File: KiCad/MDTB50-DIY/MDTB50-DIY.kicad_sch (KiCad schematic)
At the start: 18 parts

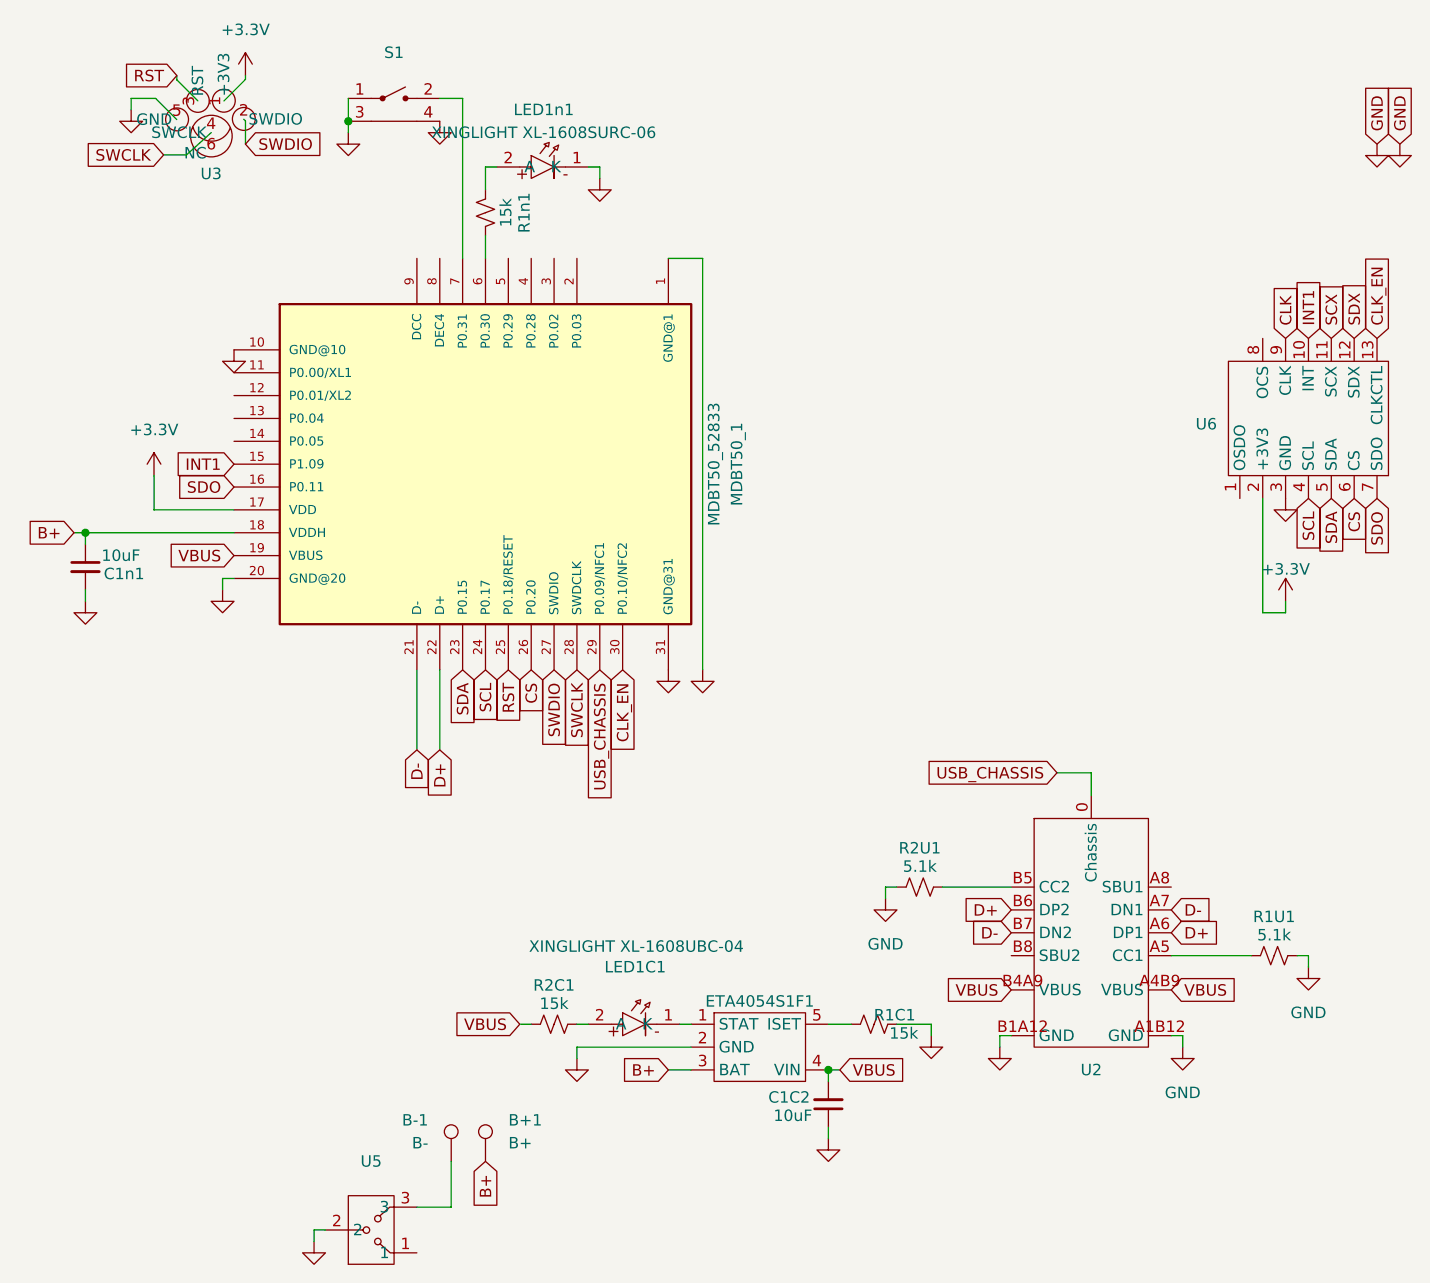
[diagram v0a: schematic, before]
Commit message: - Started redoing layout for DIY variant
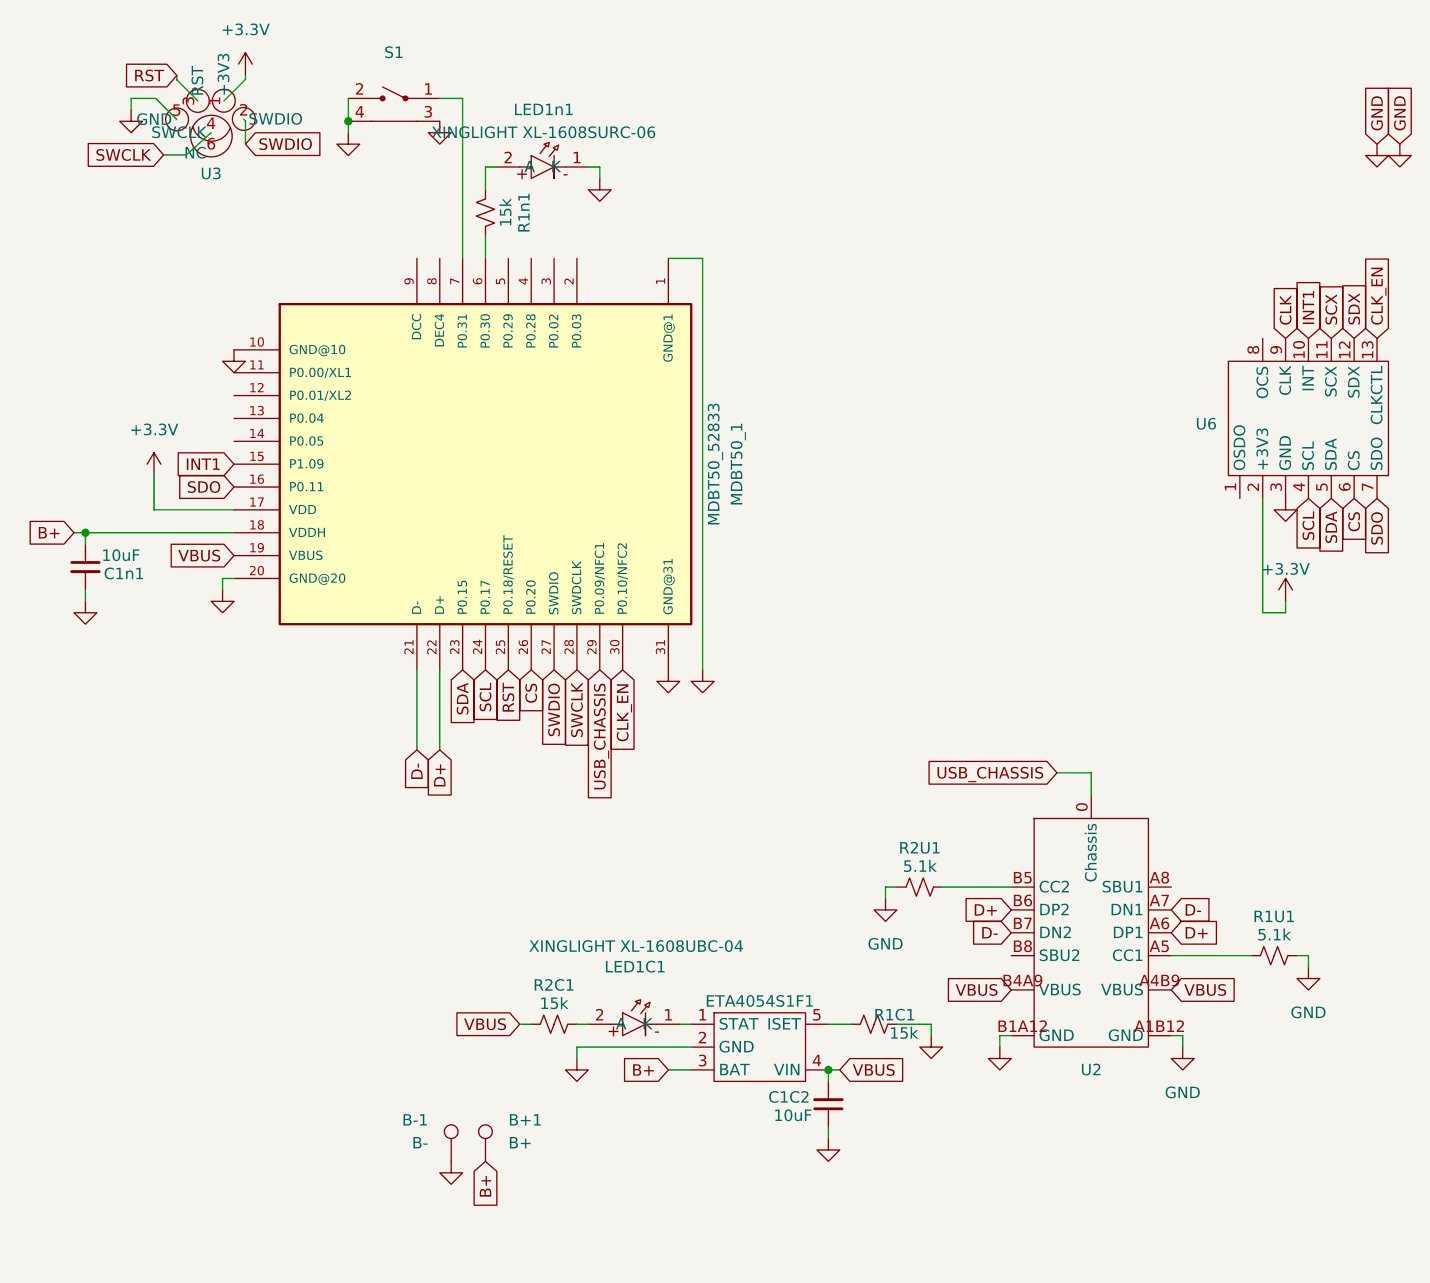
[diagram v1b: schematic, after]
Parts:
- removed U5: ~, Switch_Custom:CJS-1200TB, symbol switch-Custom2:Nidec_CJS-1200TB
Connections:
- net GND: now also B-1.1, S1.2; no longer S1.1
- net at MDBT50_1.7 (P0.31): now also S1.1; no longer S1.2
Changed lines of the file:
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@@
 	(wire
 		(pts
-			(xy 63.5 152.4) (xy 64.77 152.4)
-		)
-		(stroke
-			(width 0)
-			(type default)
-		)
-	)
-	(wire
-		(pts
 			(xy 120.65 142.24) (xy 120.65 140.97)
 		)
@@
 	(wire
 		(pts
-			(xy 63.5 152.4) (xy 63.5 153.67)
-		)
-		(stroke
-			(width 0)
-			(type default)
-		)
-	)
-	(wire
-		(pts
 			(xy 82.55 34.29) (xy 82.55 36.83)
 		)
@@
 	(wire
 		(pts
-			(xy 74.93 149.86) (xy 78.74 149.86)
-		)
-		(stroke
-			(width 0)
-			(type default)
-		)
-	)
-	(wire
-		(pts
 			(xy 45.8991 26.67) (xy 48.2477 29.0186)
 		)
@@
 	(wire
 		(pts
-			(xy 78.74 144.78) (xy 78.74 149.86)
-		)
-		(stroke
-			(width 0)
-			(type default)
-		)
-	)
-	(wire
-		(pts
 			(xy 48.26 24.13) (xy 48.26 24.6148)
 		)
@@
 	(symbol
 		(lib_id "power:GND")
-		(at 171.45 71.12 0)
-		(mirror y)
+		(at 78.74 144.78 0)
 		(unit 1)
 		(exclude_from_sim no)
@@
 		(on_board yes)
 		(dnp no)
-		(property "Reference" "#PWR010"
-			(at 171.45 77.47 0)
+		(property "Reference" "#PWR018"
+			(at 78.74 151.13 0)
 			(effects
 				(font
@@
 		)
 		(property "Value" "GND"
-			(at 171.45 75.184 0)
+			(at 78.74 148.844 0)
 			(effects
 				(font
@@
 		)
 		(property "Footprint" ""
-			(at 171.45 71.12 0)
+			(at 78.74 144.78 0)
 			(effects
 				(font
@@
 		)
 		(property "Datasheet" ""
-			(at 171.45 71.12 0)
+			(at 78.74 144.78 0)
 			(effects
 				(font
@@
 		)
 		(property "Description" "Power symbol creates a global label with name \"GND\" , ground"
-			(at 171.45 71.12 0)
+			(at 78.74 144.78 0)
 			(effects
 				(font
@@
 			(project "MDTB50-DIY"
 				(path "/fc39c71d-b4a8-40e7-814c-897ce106e5ba"
-					(reference "#PWR010")
+					(reference "#PWR018")
 					(unit 1)
 				)
@@
 	)
 	(symbol
-		(lib_id "Battery_management_custom_2:ETA4054S2F")
-		(at 113.03 132.08 0)
+		(lib_id "power:GND")
+		(at 171.45 71.12 0)
+		(mirror y)
 		(unit 1)
 		(exclude_from_sim no)
@@
 		(on_board yes)
 		(dnp no)
-		(property "Reference" "ETA4054S1F1"
-			(at 113.03 127 0)
+		(property "Reference" "#PWR010"
+			(at 171.45 77.47 0)
 			(effects
 				(font
 					(size 1.27 1.27)
 				)
+				(hide yes)
 			)
 		)
-		(property "Value" "~"
-			(at 113.03 127 0)
+		(property "Value" "GND"
+			(at 171.45 75.184 0)
 			(effects
 				(font
 					(size 1.27 1.27)
 				)
+				(hide yes)
 			)
 		)
-		(property "Footprint" "battery_management_custom:ETA4054S2F"
-			(at 113.03 132.08 0)
+		(property "Footprint" ""
+			(at 171.45 71.12 0)
 			(effects
 				(font
@@
 		)
 		(property "Datasheet" ""
-			(at 113.03 132.08 0)
+			(at 171.45 71.12 0)
 			(effects
 				(font
@@
 			)
 		)
-		(property "Description" ""
-			(at 113.03 132.08 0)
+		(property "Description" "Power symbol creates a global label with name \"GND\" , ground"
+			(at 171.45 71.12 0)
 			(effects
 				(font
@@
 			)
 		)
-		(pin "3"
-		)
-		(pin "2"
-		)
-		(pin "5"
-		)
 		(pin "1"
 		)
-		(pin "4"
-		)
 		(instances
-			(project ""
+			(project "MDTB50-DIY"
 				(path "/fc39c71d-b4a8-40e7-814c-897ce106e5ba"
-					(reference "ETA4054S1F1")
+					(reference "#PWR010")
 					(unit 1)
 				)
@@
 	)
 	(symbol
-		(lib_id "Device:R_Small_US")
-		(at 125.73 129.54 90)
+		(lib_id "Battery_management_custom_2:ETA4054S2F")
+		(at 113.03 132.08 0)
 		(unit 1)
 		(exclude_from_sim no)
@@
 		(on_board yes)
 		(dnp no)
-		(property "Reference" "R1C1"
-			(at 128.016 128.524 90)
+		(property "Reference" "ETA4054S1F1"
+			(at 113.03 127 0)
 			(effects
 				(font
@@
 			)
 		)
-		(property "Value" "15k"
-			(at 129.032 130.556 90)
+		(property "Value" "~"
+			(at 113.03 127 0)
 			(effects
 				(font
@@
 			)
 		)
-		(property "Footprint" "passive_custom:R_0402_JLC"
-			(at 125.73 129.54 0)
+		(property "Footprint" "battery_management_custom:ETA4054S2F"
+			(at 113.03 132.08 0)
 			(effects
 				(font
@@
 			)
 		)
-		(property "Datasheet" "~"
-			(at 125.73 129.54 0)
+		(property "Datasheet" ""
+			(at 113.03 132.08 0)
 			(effects
 				(font
@@
 			)
 		)
-		(property "Description" "Resistor, small US symbol"
-			(at 125.73 129.54 0)
+		(property "Description" ""
+			(at 113.03 132.08 0)
 			(effects
 				(font
@@
 			)
 		)
+		(pin "3"
+		)
 		(pin "2"
 		)
+		(pin "5"
+		)
 		(pin "1"
 		)
+		(pin "4"
+		)
 		(instances
 			(project ""
 				(path "/fc39c71d-b4a8-40e7-814c-897ce106e5ba"
-					(reference "R1C1")
+					(reference "ETA4054S1F1")
 					(unit 1)
 				)
@@
 	)
 	(symbol
-		(lib_id "switch-Custom2:Nidec_CJS-1200TB")
-		(at 69.85 152.4 90)
+		(lib_id "Device:R_Small_US")
+		(at 125.73 129.54 90)
 		(unit 1)
 		(exclude_from_sim no)
@@
 		(on_board yes)
 		(dnp no)
-		(fields_autoplaced yes)
-		(property "Reference" "U5"
-			(at 69.85 144.78 90)
+		(property "Reference" "R1C1"
+			(at 128.016 128.524 90)
 			(effects
 				(font
@@
 			)
 		)
-		(property "Value" "~"
-			(at 69.85 147.32 90)
+		(property "Value" "15k"
+			(at 129.032 130.556 90)
 			(effects
 				(font
@@
 			)
 		)
-		(property "Footprint" "Switch_Custom:CJS-1200TB"
-			(at 59.69 152.146 0)
+		(property "Footprint" "passive_custom:R_0402_JLC"
+			(at 125.73 129.54 0)
 			(effects
 				(font
@@
 			)
 		)
-		(property "Datasheet" ""
-			(at 69.85 152.4 0)
+		(property "Datasheet" "~"
+			(at 125.73 129.54 0)
 			(effects
 				(font
@@
 			)
 		)
-		(property "Description" ""
-			(at 69.85 152.4 0)
+		(property "Description" "Resistor, small US symbol"
+			(at 125.73 129.54 0)
 			(effects
 				(font
@@
 		(pin "1"
 		)
-		(pin "3"
-		)
 		(instances
 			(project ""
 				(path "/fc39c71d-b4a8-40e7-814c-897ce106e5ba"
-					(reference "U5")
+					(reference "R1C1")
 					(unit 1)
 				)
@@
 	(symbol
 		(lib_id "power:GND")
-		(at 63.5 153.67 0)
-		(unit 1)
-		(exclude_from_sim no)
-		(in_bom yes)
-		(on_board yes)
-		(dnp no)
-		(property "Reference" "#PWR027"
-			(at 63.5 160.02 0)
-			(effects
-				(font
-					(size 1.27 1.27)
-				)
-				(hide yes)
-			)
-		)
-		(property "Value" "GND"
-			(at 63.5 157.734 0)
-			(effects
-				(font
-					(size 1.27 1.27)
-				)
-				(hide yes)
-			)
-		)
-		(property "Footprint" ""
-			(at 63.5 153.67 0)
-			(effects
-				(font
-					(size 1.27 1.27)
-				)
-				(hide yes)
-			)
-		)
-		(property "Datasheet" ""
-			(at 63.5 153.67 0)
-			(effects
-				(font
-					(size 1.27 1.27)
-				)
-				(hide yes)
-			)
-		)
-		(property "Description" "Power symbol creates a global label with name \"GND\" , ground"
-			(at 63.5 153.67 0)
-			(effects
-				(font
-					(size 1.27 1.27)
-				)
-				(hide yes)
-			)
-		)
-		(pin "1"
-		)
-		(instances
-			(project "MDTB50+icm"
-				(path "/fc39c71d-b4a8-40e7-814c-897ce106e5ba"
-					(reference "#PWR027")
-					(unit 1)
-				)
-			)
-		)
-	)
-	(symbol
-		(lib_id "power:GND")
 		(at 53.34 81.28 0)
 		(unit 1)
@@
 		(lib_id "button_custom:GT-TC020B-H035-L05")
 		(at 72.39 27.94 0)
+		(mirror y)
 		(unit 1)
 		(exclude_from_sim no)
@@
 		(on_board yes)
 		(dnp no)
-		(fields_autoplaced yes)
 		(property "Reference" "S1"
 			(at 72.39 21.59 0)

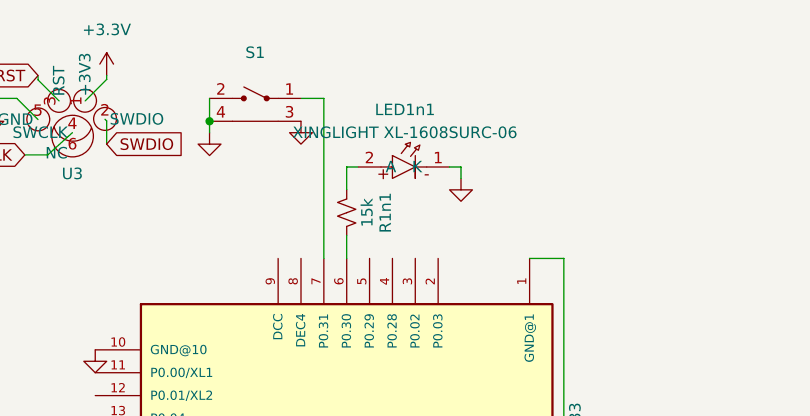
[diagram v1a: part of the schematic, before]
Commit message: - Changed PCB to 4 layer - Added QMC6309 magnetometer
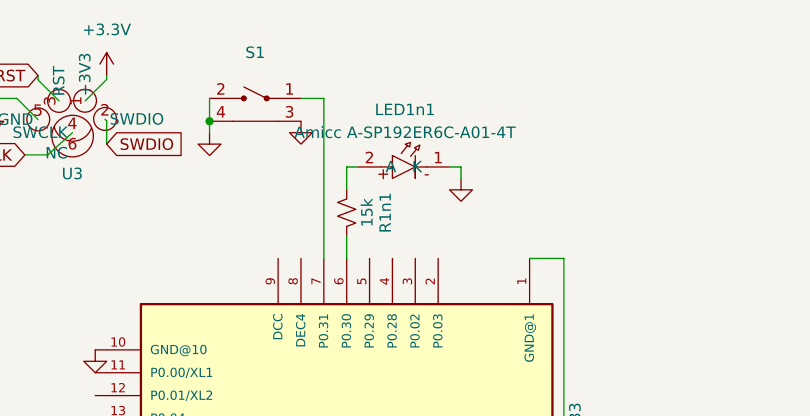
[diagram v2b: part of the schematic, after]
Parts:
- LED1n1: value XINGLIGHT XL-1608SURC-06 -> Amicc A-SP192ER6C-A01-4T
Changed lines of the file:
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@@
 			)
 		)
-		(property "Value" "XINGLIGHT XL-1608SURC-06"
+		(property "Value" "Amicc A-SP192ER6C-A01-4T"
 			(at 89.027 30.48 0)
 			(effects
